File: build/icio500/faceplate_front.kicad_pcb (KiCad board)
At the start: 4 copper layers, 38.1 x 133.3 mm, 3 parts

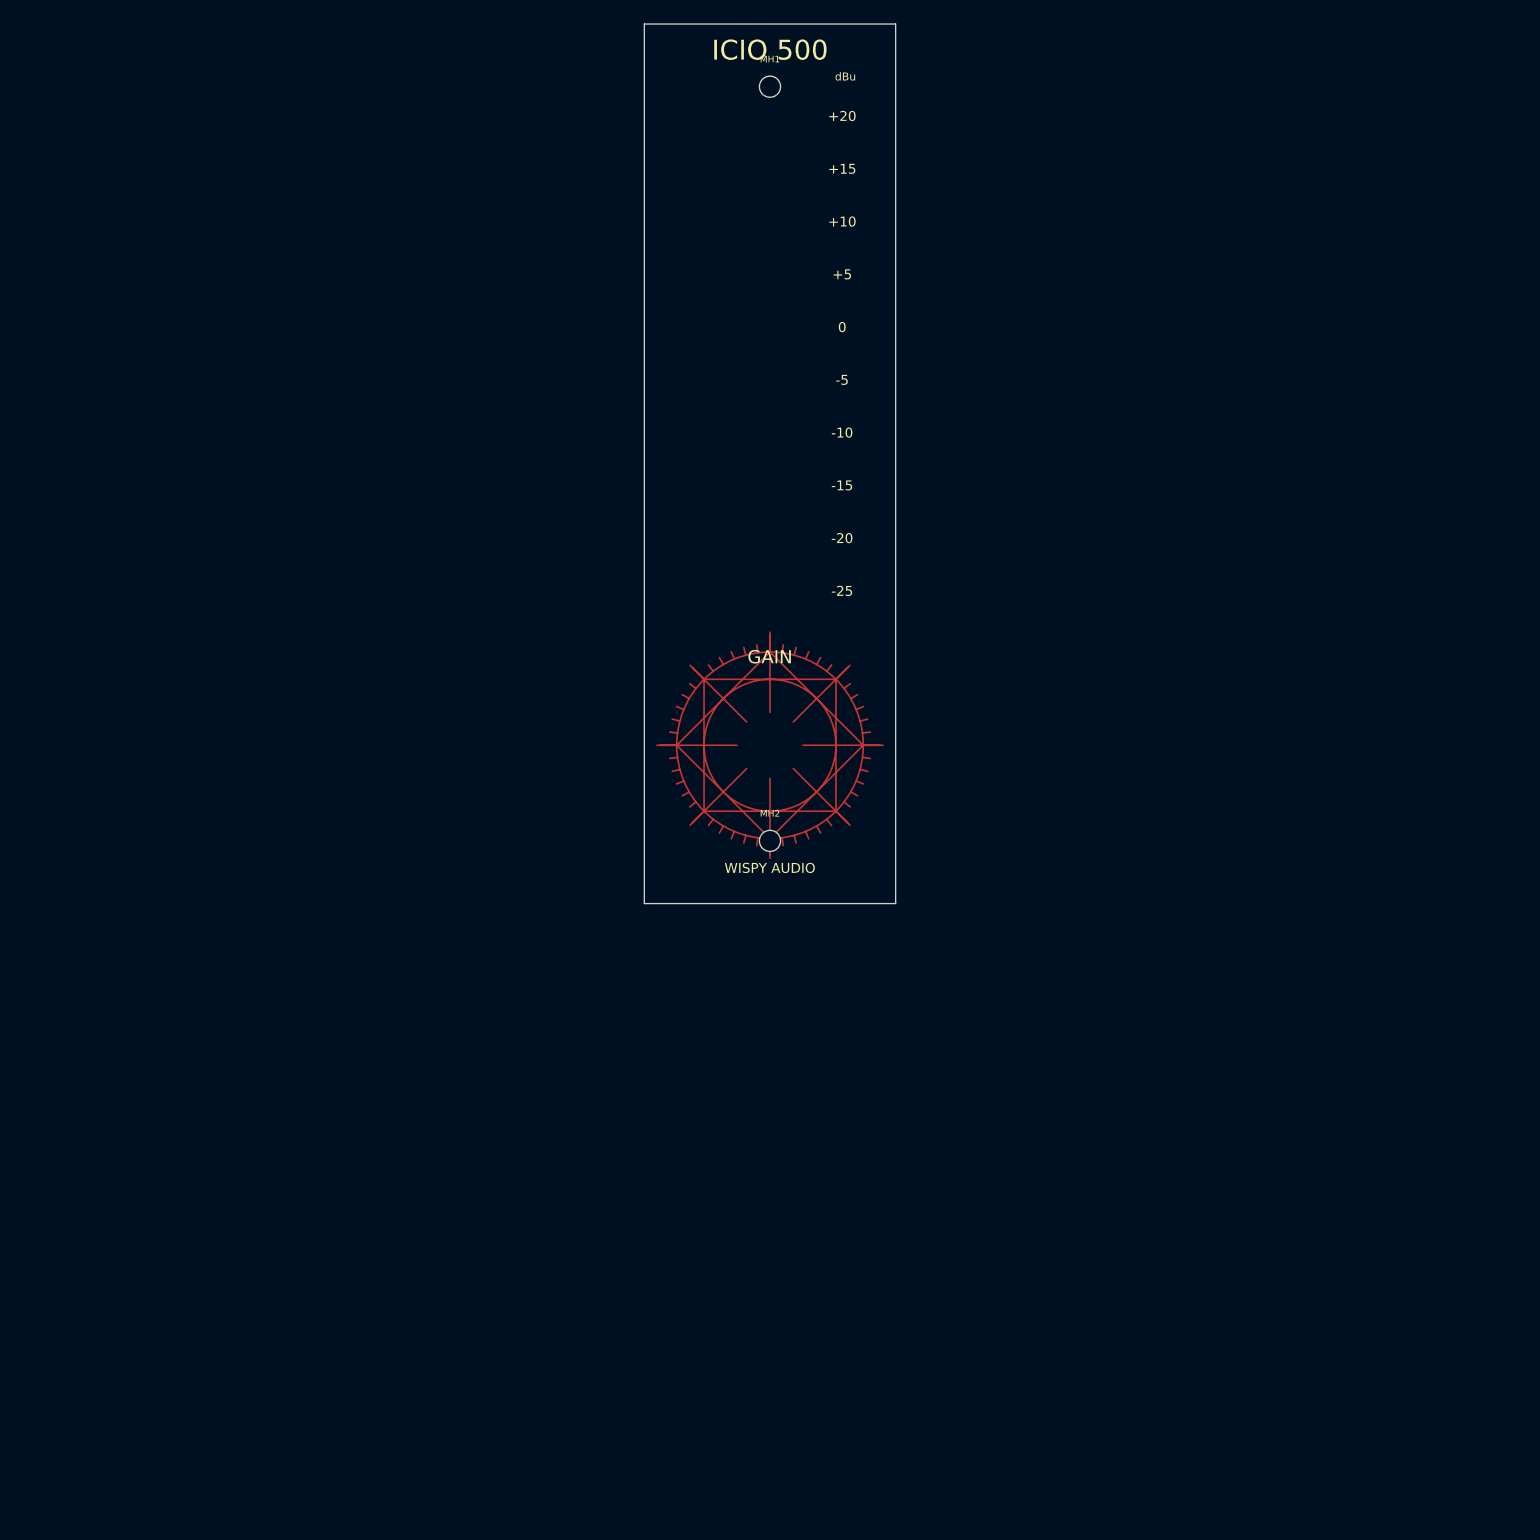
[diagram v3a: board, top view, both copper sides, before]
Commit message: Update satellite connector position and faceplate cutouts/silkscreen, regenerate STEP files
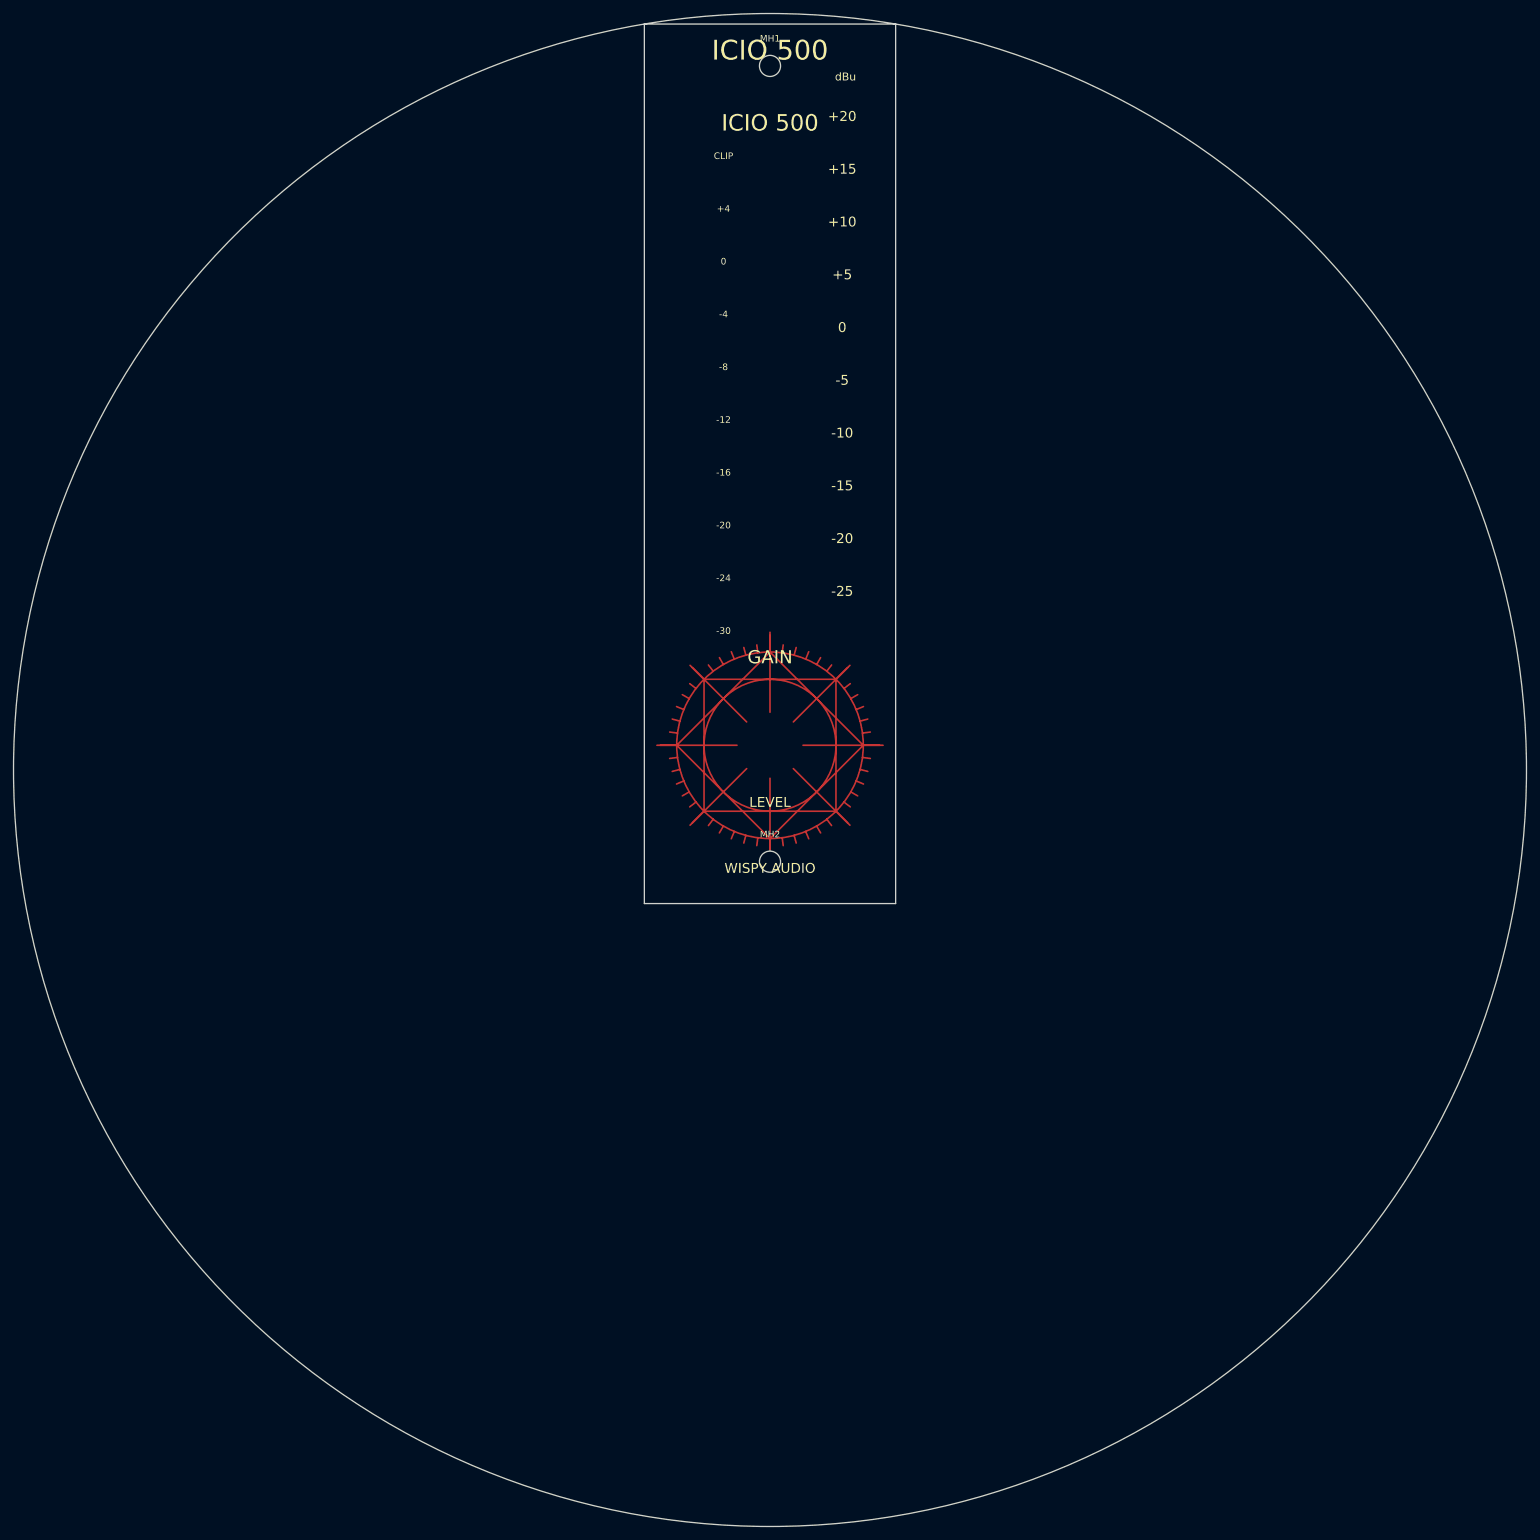
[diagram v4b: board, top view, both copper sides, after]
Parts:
- moved MH2 3.15 mm to (19.1, 127.0)
- moved MH1 3.15 mm to (19.1, 6.35)
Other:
- board size 38.1 x 133.3 mm -> 229.4 x 229.4 mm
- board text added: "+4"
- board text added: "-12"
- board text added: "-16"
- board text added: "-24"
- board text added: "-30"
- board text added: "-4"
- board text added: "-8"
- board text added: "CLIP"
- board text added: "LEVEL"
